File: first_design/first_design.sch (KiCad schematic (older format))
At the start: 34 parts

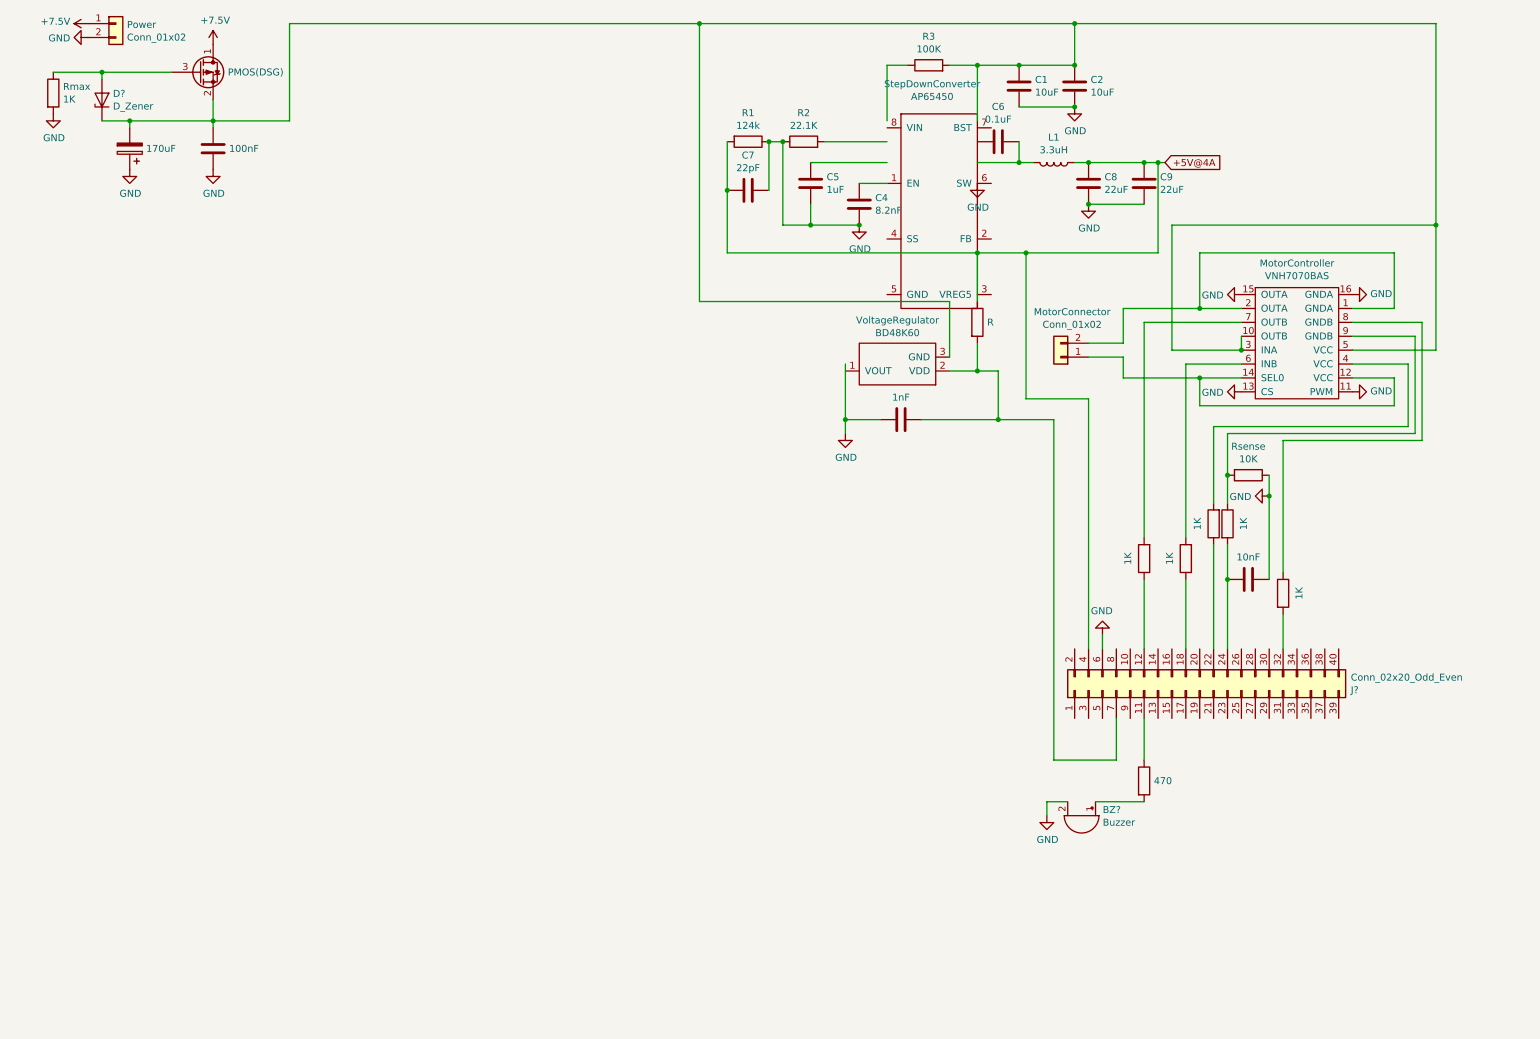
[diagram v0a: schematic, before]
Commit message: labels added
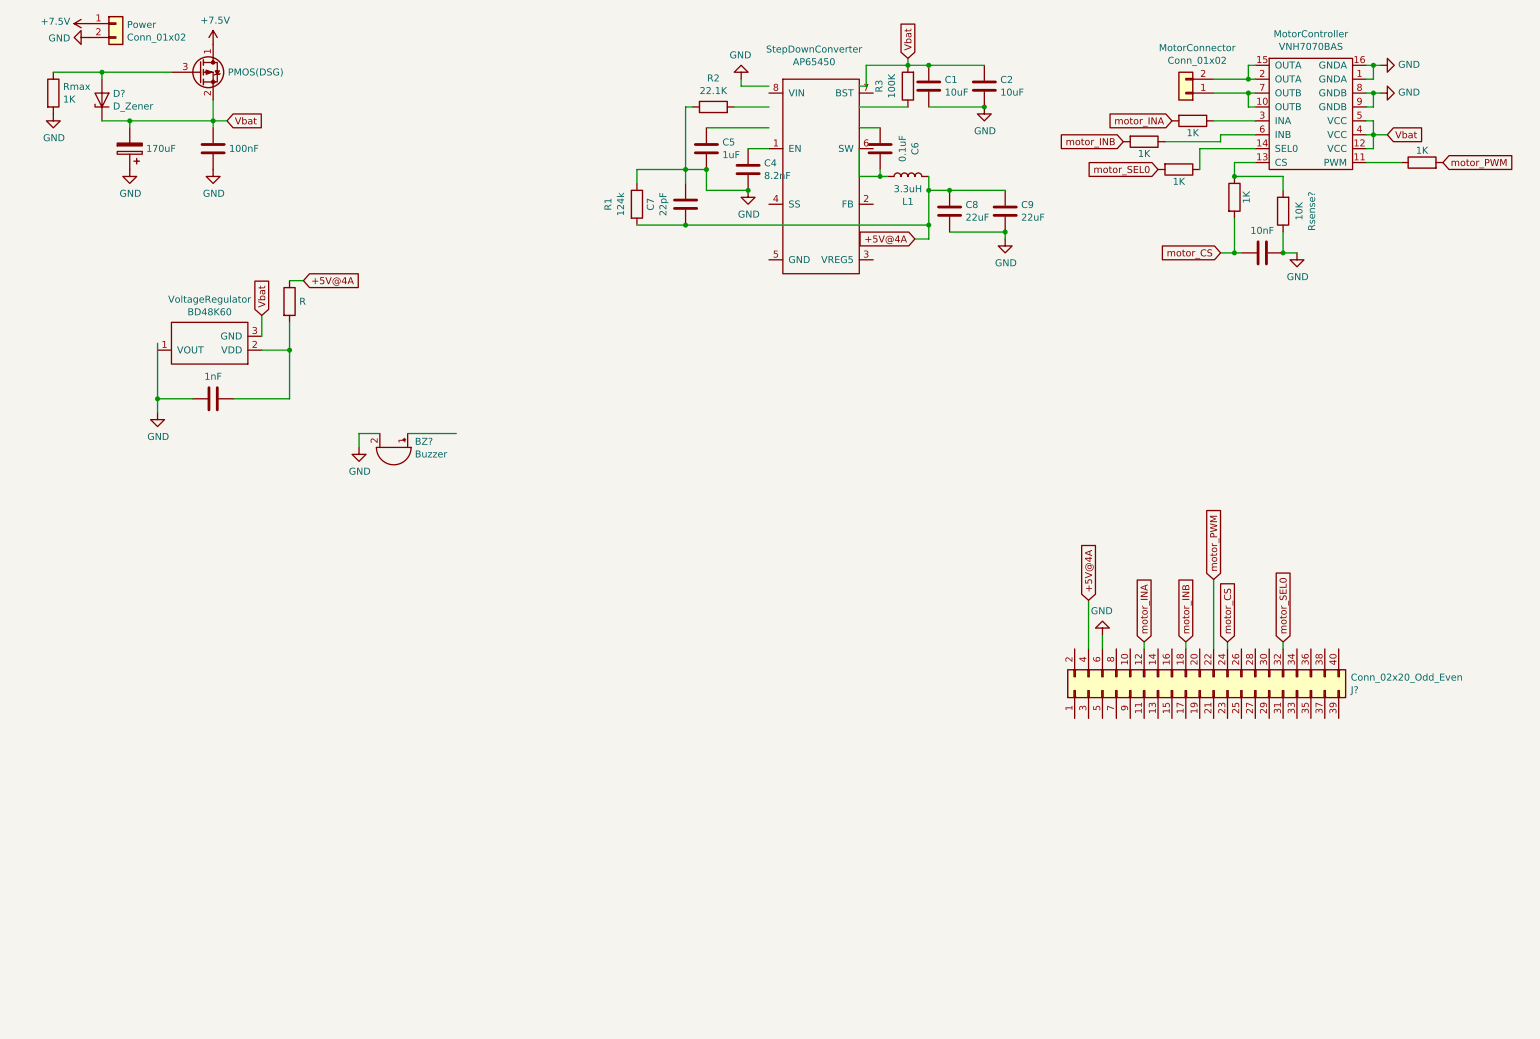
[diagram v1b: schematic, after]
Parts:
- removed C?: 10nF, symbol Device:C
- removed R? (x4): 1K, symbol Device:R
- removed R?: 470, symbol Device:R
- removed Rsense: 10K, symbol Device:R
- added C?: 10nF, symbol Device:C
- added R? (x4): 1K, symbol Device:R
- added Rsense?: 10K, symbol Device:R
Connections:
- net labels added: Vbat, motor_CS, motor_INA, motor_INB, motor_PWM, motor_SEL0
- wire segments 116 -> 102
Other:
- moved on the sheet: BZ?, C1, C2, MotorConnector, VoltageRegulator

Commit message: buzzer layout + buttons added
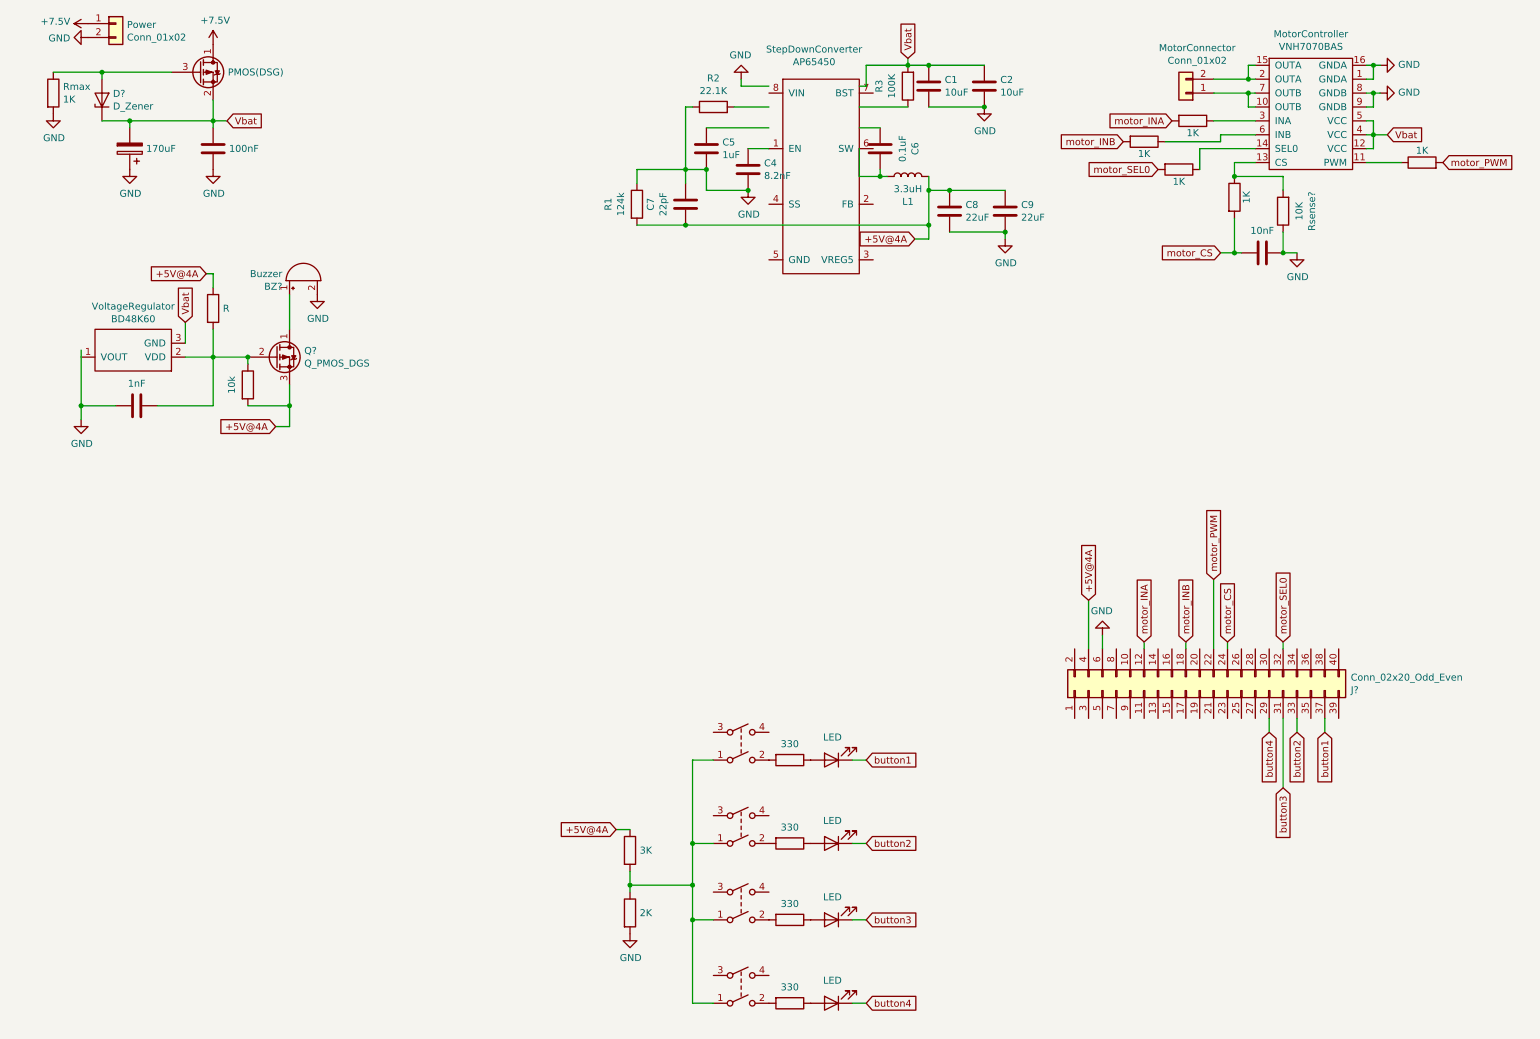
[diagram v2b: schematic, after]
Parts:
- added D? (x4): LED, symbol Device:LED
- added Q?: Q_PMOS_DGS, symbol Device:Q_PMOS_DGS
- added R? (x4): 330, symbol Device:R
- added R?: 3K, symbol Device:R
- added R?: 2K, symbol Device:R
- added R?: 10k, symbol Device:R
- added SW? (x4): SW_DPST, symbol Switch:SW_DPST
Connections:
- net labels added: button1, button2, button3, button4
- wire segments 102 -> 127
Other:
- moved on the sheet: BZ?, VoltageRegulator

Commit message: IR Circuit added
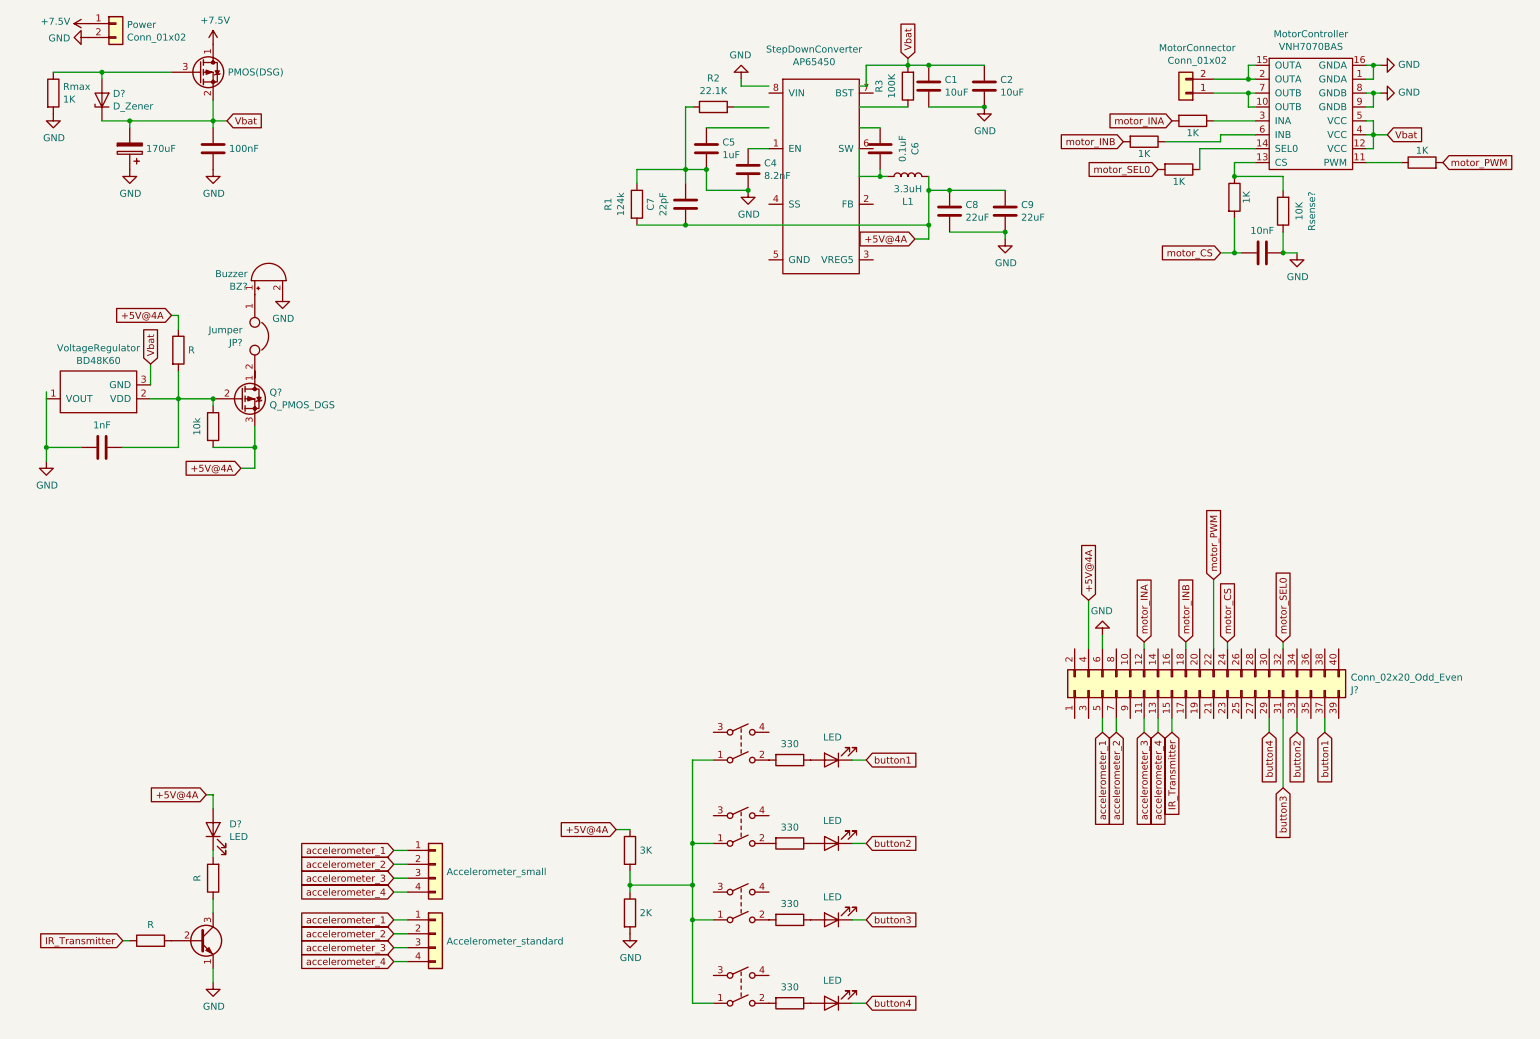
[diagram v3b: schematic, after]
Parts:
- added D?: LED, symbol Device:LED
- added J?: Accelerometer_small, symbol Connector_Generic:Conn_01x04
- added J?: Accelerometer_standard, symbol Connector_Generic:Conn_01x04
- added JP?: Jumper, symbol Device:Jumper
- added Q?: BJT, symbol Transistor_BJT:2N2219
- added R? (x2): R, symbol Device:R
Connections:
- net labels added: IR_Transmitter, accelerometer_1, accelerometer_2, accelerometer_3, accelerometer_4
- wire segments 127 -> 145
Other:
- moved on the sheet: BZ?, Q?, VoltageRegulator

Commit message: IR circuit fix
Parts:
- removed R?: R, symbol Device:R
- added Q?: 2N4403, symbol Device:Q_PNP_BCE
- added R?: 270, symbol Device:R
- R?: value R -> 34
- gave numbers to parts that had none: 2
- renumbered VoltageRegulator to VoltageMonitor
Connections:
- wire segments 145 -> 148
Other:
- moved on the sheet: SFH4845
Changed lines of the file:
@@
 	1300 3250 1500 3250
 $Comp
-L Sensor_Voltage:BD48K60 VoltageRegulator
+L Sensor_Voltage:BD48K60 VoltageMonitor
 U 1 1 5D1051D4
 P 900 3100
-F 0 "VoltageRegulator" H 875 2885 50  0000 C CNN
+F 0 "VoltageMonitor" H 875 2885 50  0000 C CNN
 F 1 "BD48K60" H 875 2976 50  0000 C CNN
 F 2 "" H 900 3000 50  0001 C CNN
@@
 Text GLabel 8650 5650 3    50   Input ~ 0
 IR_Transmitter
-Text GLabel 1100 7150 0    50   Input ~ 0
+Text GLabel 1650 7600 0    50   Input ~ 0
 IR_Transmitter
 $Comp
-L Device:R R?
-U 1 1 5D4D4634
-P 1300 7150
-F 0 "R?" H 1370 7196 50  0001 L CNN
-F 1 "R" V 1415 7150 50  0000 C CNN
-F 2 "" V 1230 7150 50  0001 C CNN
-F 3 "~" H 1300 7150 50  0001 C CNN
-	1    1300 7150
+L Transistor_BJT:2N2219 2N4401
+U 1 1 5D4DF047
+P 1750 7300
+F 0 "2N4401" H 1940 7300 50  0000 L CNN
+F 1 "BJT" H 1940 7255 50  0001 L CNN
+F 2 "" H 1950 7225 50  0001 L CIN
+F 3 "http://www.onsemi.com/pub_link/Collateral/2N2219-D.PDF" H 1750 7300 50  0001 L CNN
+	1    1750 7300
 	0    -1   -1   0
 $EndComp
-Wire Wire Line
-	1100 7150 1150 7150
-$Comp
-L Transistor_BJT:2N2219 Q?
-U 1 1 5D4DF047
-P 1650 7150
-F 0 "Q?" H 1840 7196 50  0001 L CNN
-F 1 "BJT" H 1840 7105 50  0001 L CNN
-F 2 "" H 1850 7075 50  0001 L CIN
-F 3 "http://www.onsemi.com/pub_link/Collateral/2N2219-D.PDF" H 1650 7150 50  0001 L CNN
-	1    1650 7150
-	1    0    0    -1
-$EndComp
 $Comp
 L power:GND #PWR?
 U 1 1 5D4DFD4B
-P 1750 7450
-F 0 "#PWR?" H 1750 7200 50  0001 C CNN
-F 1 "GND" H 1755 7277 50  0000 C CNN
-F 2 "" H 1750 7450 50  0001 C CNN
-F 3 "" H 1750 7450 50  0001 C CNN
-	1    1750 7450
-	1    0    0    -1
-$EndComp
-Wire Wire Line
-	1750 7350 1750 7450
-$Comp
-L Device:LED D?
+P 600 6700
+F 0 "#PWR?" H 600 6450 50  0001 C CNN
+F 1 "GND" H 605 6527 50  0000 C CNN
+F 2 "" H 600 6700 50  0001 C CNN
+F 3 "" H 600 6700 50  0001 C CNN
+	1    600  6700
+	1    0    0    -1
+$EndComp
+$Comp
+L Device:LED SFH4845
 U 1 1 5D4E5B7A
-P 1750 6350
-F 0 "D?" V 1789 6233 50  0000 R CNN
-F 1 "LED" V 1698 6233 50  0000 R CNN
-F 2 "" H 1750 6350 50  0001 C CNN
-F 3 "~" H 1750 6350 50  0001 C CNN
-	1    1750 6350
+P 1200 6600
+F 0 "SFH4845" V 1239 6482 50  0000 R CNN
+F 1 "LED" V 1148 6482 50  0000 R CNN
+F 2 "" H 1200 6600 50  0001 C CNN
+F 3 "~" H 1200 6600 50  0001 C CNN
+	1    1200 6600
+	1    0    0    -1
+$EndComp
+$Comp
+L Device:R R?
+U 1 1 5D4FCBFC
+P 850 6600
+F 0 "R?" H 920 6646 50  0001 L CNN
+F 1 "34" H 780 6600 50  0000 R CNN
+F 2 "" V 780 6600 50  0001 C CNN
+F 3 "~" H 850 6600 50  0001 C CNN
+	1    850  6600
 	0    -1   -1   0
 $EndComp
 Wire Wire Line
-	1750 6850 1750 6950
-Text GLabel 1700 6100 0    50   Input ~ 0
-+5V@4A
-Wire Wire Line
-	1700 6100 1750 6100
-Wire Wire Line
-	1750 6100 1750 6200
-$Comp
-L Device:R R?
-U 1 1 5D4FCBFC
-P 1750 6700
-F 0 "R?" H 1820 6746 50  0001 L CNN
-F 1 "R" V 1865 6700 50  0000 C CNN
-F 2 "" V 1680 6700 50  0001 C CNN
-F 3 "~" H 1750 6700 50  0001 C CNN
-	1    1750 6700
-	-1   0    0    1
-$EndComp
-Wire Wire Line
-	1750 6500 1750 6550
+	1050 6600 1000 6600
 $Comp
 L Connector_Generic:Conn_01x04 J?
@@
 Wire Wire Line
 	8150 5550 8150 5650
+Wire Wire Line
+	1750 7500 1750 7600
+$Comp
+L Device:R R?
+U 1 1 5D5D9A68
+P 2100 7200
+F 0 "R?" H 2170 7246 50  0001 L CNN
+F 1 "270" H 2030 7200 50  0000 R CNN
+F 2 "" V 2030 7200 50  0001 C CNN
+F 3 "~" H 2100 7200 50  0001 C CNN
+	1    2100 7200
+	0    1    1    0
+$EndComp
+Wire Wire Line
+	1650 7600 1750 7600
+$Comp
+L Device:Q_PNP_BCE Q?
+U 1 1 5D5E744F
+P 1550 6700
+F 0 "Q?" H 1740 6746 50  0001 L CNN
+F 1 "2N4403" H 1740 6700 50  0000 L CNN
+F 2 "" H 1750 6800 50  0001 C CNN
+F 3 "~" H 1550 6700 50  0001 C CNN
+	1    1550 6700
+	0    -1   -1   0
+$EndComp
+Text GLabel 1750 6600 2    50   Input ~ 0
++5V@4A
+Wire Wire Line
+	1550 6900 1550 7200
+Wire Wire Line
+	2250 7200 2250 6150
+Wire Wire Line
+	2250 6150 600  6150
+Wire Wire Line
+	600  6150 600  6600
+Wire Wire Line
+	700  6600 600  6600
+Connection ~ 600  6600
+Wire Wire Line
+	600  6600 600  6700
 $EndSCHEMATC
